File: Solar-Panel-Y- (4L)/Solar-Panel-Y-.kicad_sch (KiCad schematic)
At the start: 77 parts, among them J1 FTS-105-01-L-DV-A, J2 BM02B-SRSS-TB, Q1 BSS138DWQ-7, Q2 MBT2222ADW1T1, Q3 BSS138DWQ-7, Q4 MBT2222ADW1T1, SW1 D2F-L2-A1, SW2 D2F-L2-A, U1 BQ25570RGRR, U2 TSL2561

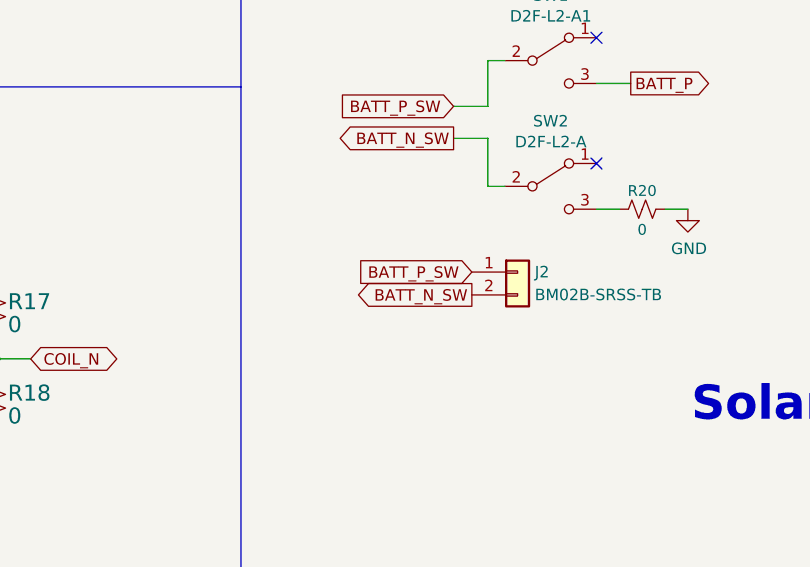
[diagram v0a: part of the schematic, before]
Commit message: Z- board antenna updates
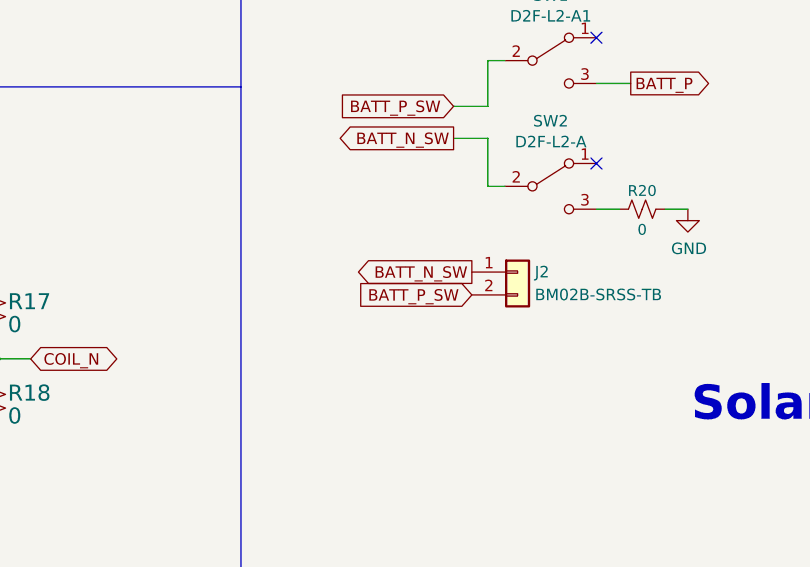
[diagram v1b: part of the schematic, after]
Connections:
- net BATT_N_SW: now also J2.1 (Pin_1); no longer J2.2 (Pin_2)
- net BATT_P_SW: now also J2.2 (Pin_2); no longer J2.1 (Pin_1)
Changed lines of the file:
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@@
     )
   )
-  (global_label "BATT_N_SW" (shape output) (at 234.442 168.148 180) (fields_autoplaced)
+  (global_label "BATT_N_SW" (shape output) (at 234.442 165.608 180) (fields_autoplaced)
     (effects (font (size 1.27 1.27)) (justify right))
-    (property "Intersheet References" "${INTERSHEET_REFS}" (id 0) (at 221.8973 168.2274 0)
+    (property "Intersheet References" "${INTERSHEET_REFS}" (id 0) (at 221.8973 165.6874 0)
       (effects (font (size 1.27 1.27)) (justify right) hide)
     )
@@
     )
   )
-  (global_label "BATT_P_SW" (shape input) (at 234.442 165.608 180) (fields_autoplaced)
+  (global_label "BATT_P_SW" (shape input) (at 234.442 168.148 180) (fields_autoplaced)
     (effects (font (size 1.27 1.27)) (justify right))
-    (property "Intersheet References" "${INTERSHEET_REFS}" (id 0) (at 221.9578 165.5286 0)
+    (property "Intersheet References" "${INTERSHEET_REFS}" (id 0) (at 221.9578 168.0686 0)
       (effects (font (size 1.27 1.27)) (justify right) hide)
     )

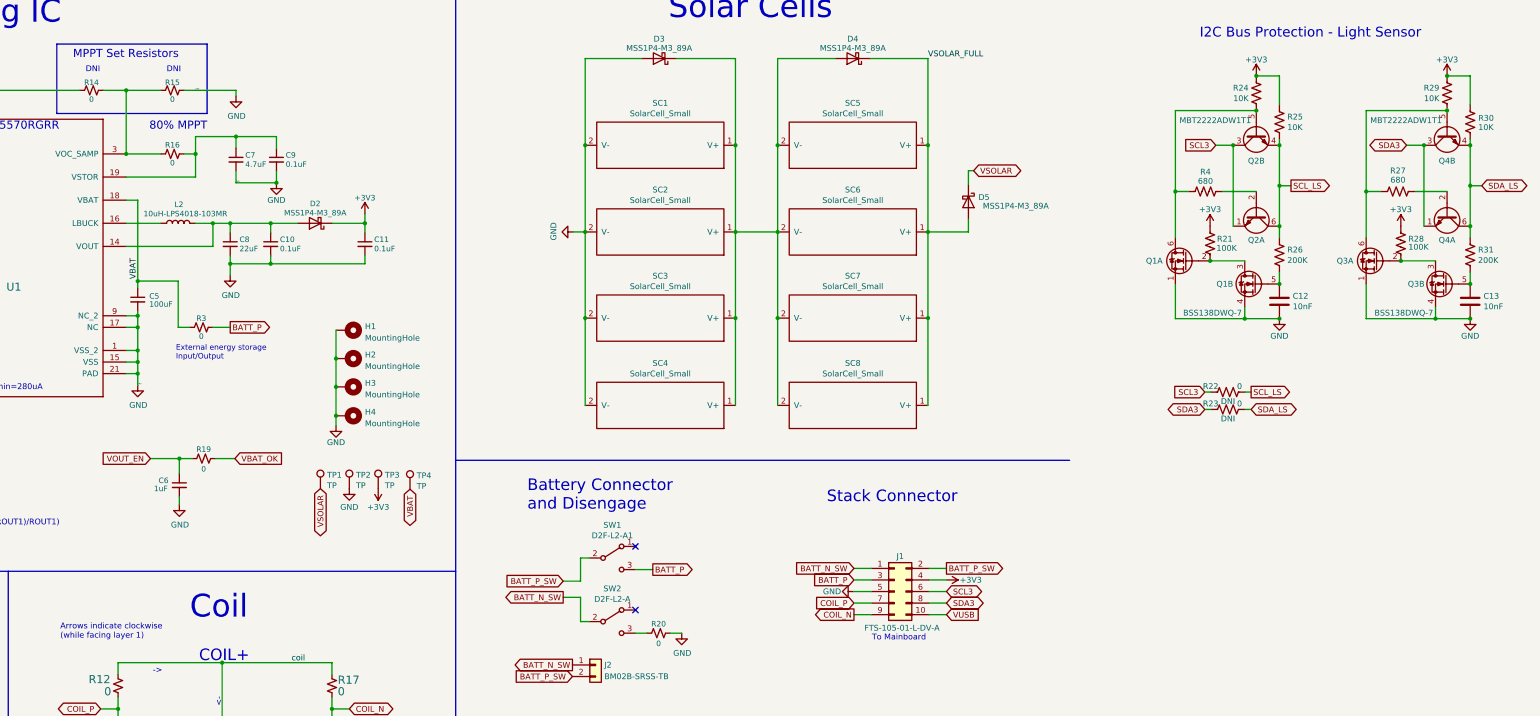
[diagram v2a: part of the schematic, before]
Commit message: Updated all solar panels to Rev B2/01 + Export STEP / BOM
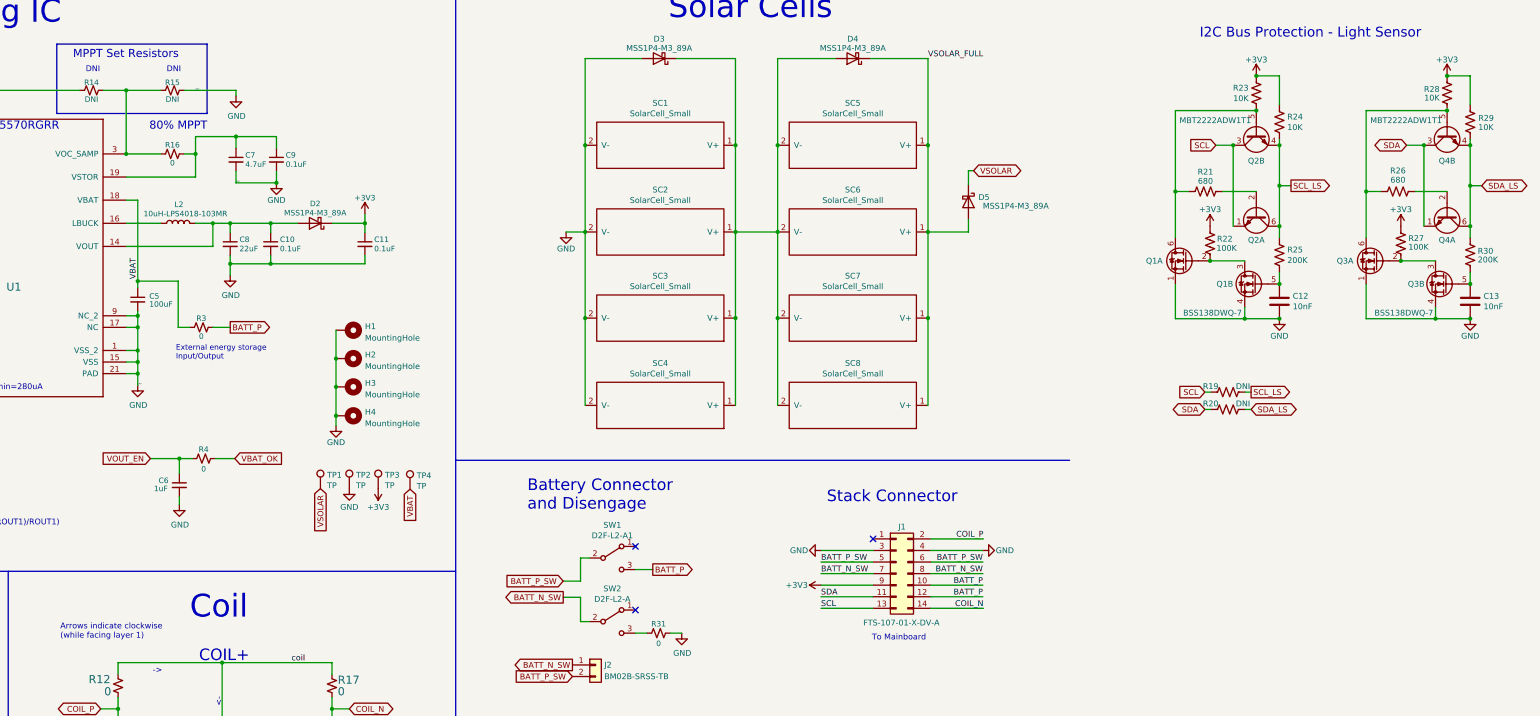
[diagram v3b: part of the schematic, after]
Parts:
- removed J1: FTS-105-01-L-DV-A, batteryboard:FTS-105-XX-YY-DV-A, symbol Connector_Generic:Conn_02x05_Odd_Even
- added J1: FTS-107-01-X-DV-A, batteryboard:SAMTEC-FTS-107-01-X-DV-A, symbol Connector_Generic:Conn_02x07_Odd_Even
- C10, C11, C12, C13, C2, C3, C4, C6, C7, C8, C9: footprint Capacitor_SMD:C_0402_1005Metric -> Capacitor_SMD:C_0603_1608Metric
- R10, R11, R12, R13, R16, R17, R18, R3, R5, R6, R7, R8, R9: footprint Resistor_SMD:R_0402_1005Metric -> Resistor_SMD:R_0603_1608Metric
- R14, R15: value 0 -> DNI; footprint Resistor_SMD:R_0402_1005Metric -> Resistor_SMD:R_0603_1608Metric
- R19: renamed from R22; value 0 -> DNI; footprint Resistor_SMD:R_0402_1005Metric -> Resistor_SMD:R_0603_1608Metric
- R20: renamed from R23; value 0 -> DNI; footprint Resistor_SMD:R_0402_1005Metric -> Resistor_SMD:R_0603_1608Metric
- R21: renamed from R4; footprint Resistor_SMD:R_0402_1005Metric -> Resistor_SMD:R_0603_1608Metric
- R22: renamed from R21; footprint Resistor_SMD:R_0402_1005Metric -> Resistor_SMD:R_0603_1608Metric
- R23: renamed from R24; footprint Resistor_SMD:R_0402_1005Metric -> Resistor_SMD:R_0603_1608Metric
- R24: renamed from R25; footprint Resistor_SMD:R_0402_1005Metric -> Resistor_SMD:R_0603_1608Metric
- R25: renamed from R26; footprint Resistor_SMD:R_0402_1005Metric -> Resistor_SMD:R_0603_1608Metric
- R26: renamed from R27; footprint Resistor_SMD:R_0402_1005Metric -> Resistor_SMD:R_0603_1608Metric
- R27: renamed from R28; footprint Resistor_SMD:R_0402_1005Metric -> Resistor_SMD:R_0603_1608Metric
- R28: renamed from R29; footprint Resistor_SMD:R_0402_1005Metric -> Resistor_SMD:R_0603_1608Metric
- R29: renamed from R30; footprint Resistor_SMD:R_0402_1005Metric -> Resistor_SMD:R_0603_1608Metric
- R30: renamed from R31; footprint Resistor_SMD:R_0402_1005Metric -> Resistor_SMD:R_0603_1608Metric
- R31: renamed from R20; footprint Resistor_SMD:R_0402_1005Metric -> Resistor_SMD:R_0603_1608Metric
- R4: renamed from R19; footprint Resistor_SMD:R_0402_1005Metric -> Resistor_SMD:R_0603_1608Metric
- renumbered SC3 to SC2, SC2 to SC3
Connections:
- net +3V3: now also J1.9 (Pin_9)
- net BATT_N_SW: now also J1.7 (Pin_7), J1.8 (Pin_8)
- net BATT_P: now also J1.10 (Pin_10), J1.12 (Pin_12)
- net BATT_P_SW: now also J1.5 (Pin_5), J1.6 (Pin_6)
- net COIL_N: now also J1.14 (Pin_14)
- net COIL_P: now also J1.2 (Pin_2)
- net GND: now also J1.3 (Pin_3), J1.4 (Pin_4)
- net SCL3 renamed SCL
- net SCL: now also J1.13 (Pin_13)
- net SDA3 renamed SDA
- net SDA: now also J1.11 (Pin_11)
- no-connect marks 3 -> 4
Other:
- moved on the sheet: SC2, SC3

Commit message: Y- board changes for Rev B3/01
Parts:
- removed C12, C13: 10nF, Capacitor_SMD:C_0603_1608Metric, symbol Device:C
- removed Q1, Q3: BSS138DWQ-7, Package_TO_SOT_SMD:SOT-363_SC-70-6, symbol mainboard:BSS138DWQ-7
- removed Q2, Q4: MBT2222ADW1T1, Package_TO_SOT_SMD:SOT-363_SC-70-6, symbol Transistor_BJT:MBT2222ADW1T1
- removed R19, R20: DNI, Resistor_SMD:R_0603_1608Metric, symbol Device:R_US
- removed R21, R26: 680, Resistor_SMD:R_0603_1608Metric, symbol Device:R_US
- removed R22, R27: 100K, Resistor_SMD:R_0603_1608Metric, symbol Device:R_US
- removed R23, R24, R28, R29: 10K, Resistor_SMD:R_0603_1608Metric, symbol Device:R_US
- removed R25, R30: 200K, Resistor_SMD:R_0603_1608Metric, symbol Device:R_US
- added C14: 1uF, Capacitor_SMD:C_0603_1608Metric, symbol Device:C_Small
- added R32: 1K, Resistor_SMD:R_0603_1608Metric, symbol Device:R_Small_US
- J2: symbol Connector_Generic:Conn_01x02 -> solarpanels:BM02B-SRSS-TB
- R1, R12, R13, R16, R17, R18, R2, R3, R31, R4: value 0 -> 0R
- R14, R15: value DNI -> DNI (0R)
- U2: value TSL2561 -> BH1750FVI; footprint solarpanels:TSL2561 -> solarpanels:BH1750FVI; symbol solarpanels:symbols_TSL2561 -> solarpanels:BH1750; Height 1.55 -> (none); Manufacturer_Name ams -> (none); Manufacturer_Part_Number TSL2561 -> (none); Mouser Part Number N/A -> (none); Mouser Price/Stock https://www.mouser.com/Search/Refine.aspx?Keyword=N%2FA -> (none)
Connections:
- net +3V3: now also R32.2
- net BATT_P: now also J1.1 (Pin_1), J1.3 (Pin_3); no longer J1.10 (Pin_10), J1.12 (Pin_12)
- net GND: now also J1.10 (Pin_10), J2.MP, U2.7 (GND), C14.1; no longer J1.3 (Pin_3)
- net SCL_LS: now also U2.6 (SCL); no longer U2.4 (SCL)
- net SDA_LS: now also U2.4 (SDA); no longer U2.6 (SDA)
- net at U2.5 (DVI): now also C14.2, R32.1
- no-connect marks 4 -> 3
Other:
- added sheet Bus Protection (BusProtection.kicad_sch)
- note added: "Populate R1 for I2C addr 0x5C, OR Populate R2 for I2C addr 0x23"
- note removed: "I2C Bus Protection - Light Sensor"
- moved on the sheet: C1, R1, R12, R13, R17, R18, R2

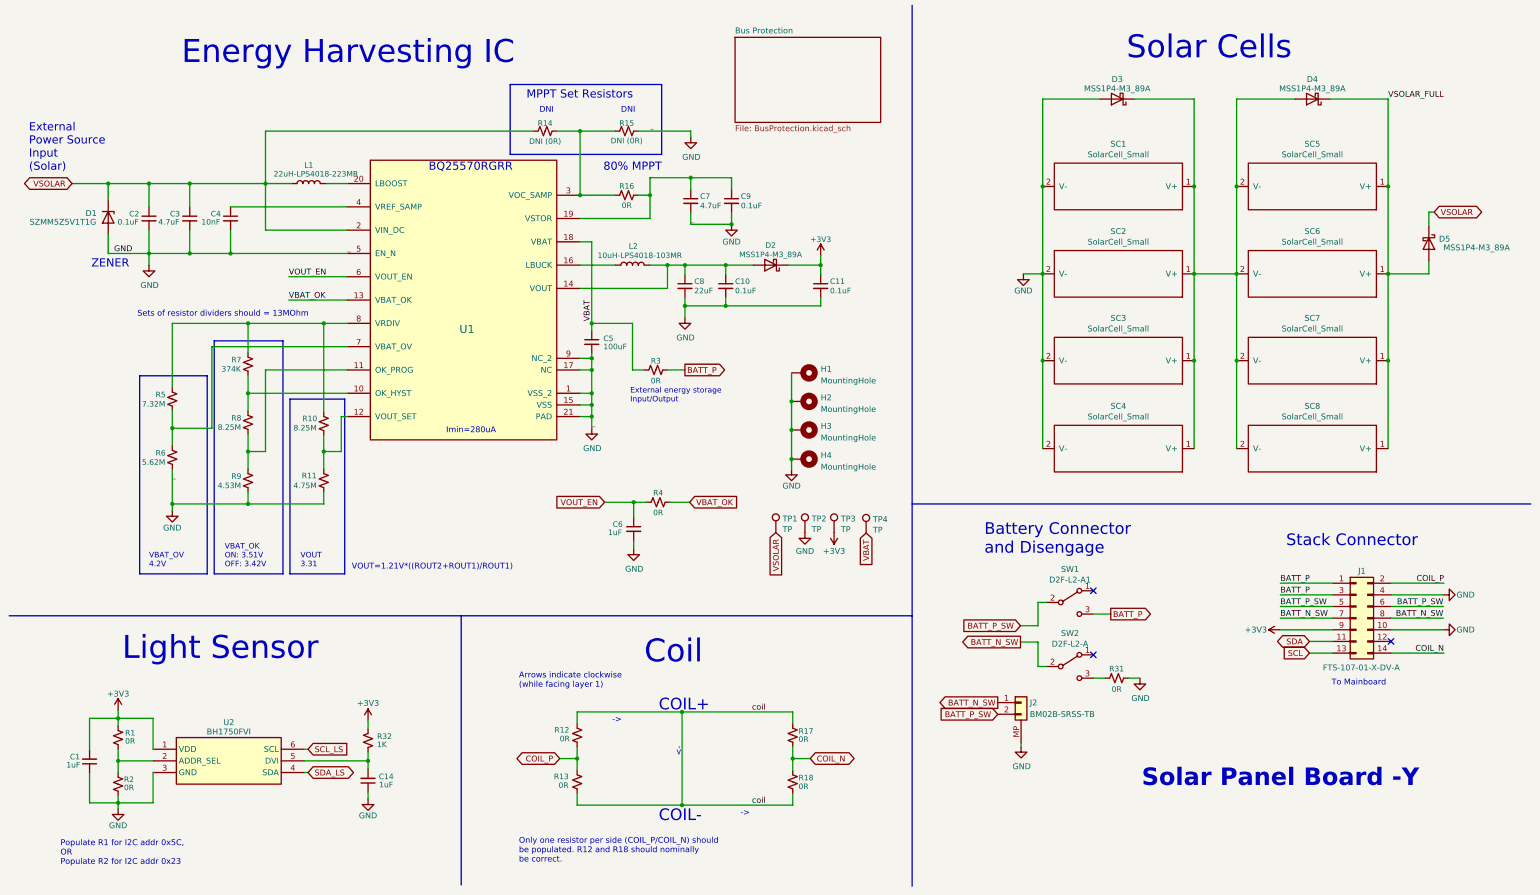
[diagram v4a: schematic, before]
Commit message: Updated light sensor to OPT 3001, Updated solar diodes.
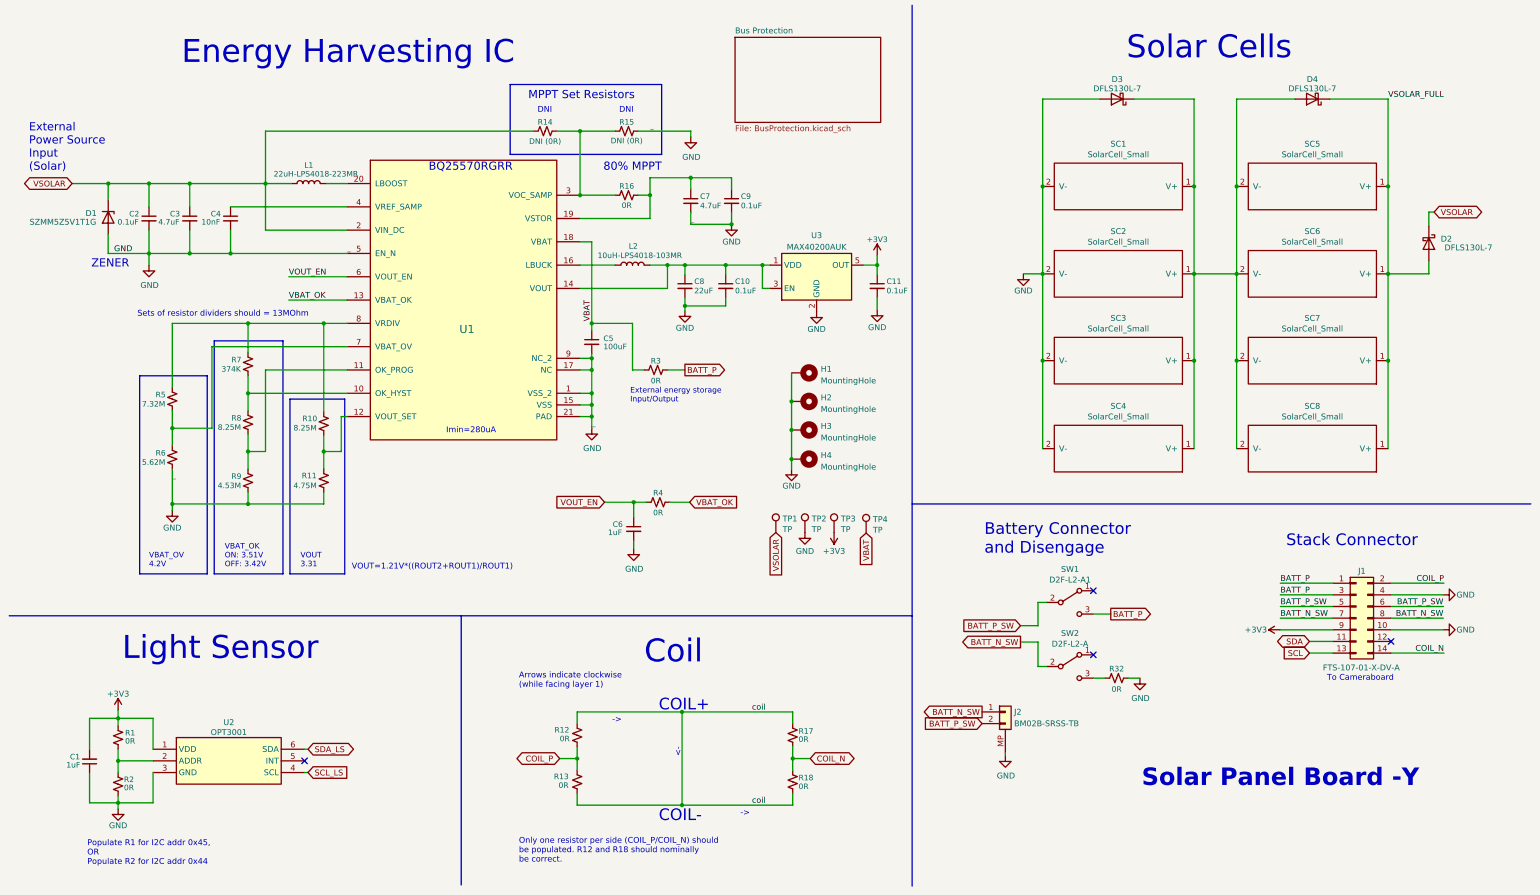
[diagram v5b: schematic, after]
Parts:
- removed C14: 1uF, Capacitor_SMD:C_0603_1608Metric, symbol Device:C_Small
- removed D5: MSS1P4-M3_89A, solarpanels:MICROSMP, symbol Device:D_Schottky
- removed R32: 1K, Resistor_SMD:R_0603_1608Metric, symbol Device:R_Small_US
- removed U2: BH1750FVI, solarpanels:BH1750FVI, symbol solarpanels:BH1750
- added U2: OPT3001, solarpanels:OPT3001, symbol solarpanels:OPT3001
- added U3: MAX40200AUK, Package_TO_SOT_SMD:SOT-23-5, symbol Analog_Switch:MAX40200AUK
- D2, D3, D4: value MSS1P4-M3_89A -> DFLS130L-7; footprint solarpanels:MICROSMP -> Diode_SMD:D_PowerDI-123; Allied Price/Stock https://www.alliedelec.com/general-semiconductor-vishay-mss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 -> (none); Allied_Number 70217632 -> (none); Manufacturer_Name Vishay -> (none); Manufacturer_Part_Number MSS1P4-M3/89A -> (none); Mouser Part Number 625-MSS1P4-M3 -> (none); Mouser Price/Stock https://www.mouser.com/Search/Refine.aspx?Keyword=625-MSS1P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 -> (none); RS Part Number 7103068P -> (none); RS Price/Stock http://uk.rs-online.com/web/p/products/7103068P -> (none)
- renumbered R31 to R32
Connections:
- net +3V3: now also U2.1 (VDD), U3.5 (OUT); no longer D2.1 (K)
- net GND: now also U2.3 (GND), U2.7 (GND), U3.2 (GND)
- net SCL_LS: now also U2.4 (SCL)
- net SDA_LS: now also U2.6 (SDA)
- net VSOLAR: now also D2.1 (K)
- net VSOLAR_FULL: now also D2.2 (A)
- net at R1.1, R2.2: now also U2.2 (ADDR)
- net at C10.1, C8.1, L2.2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: now also U3.1 (VDD), U3.3 (EN); no longer D2.2 (A)
- no-connect marks 3 -> 4
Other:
- note added: "Populate R1 for I2C addr 0x45, OR Populate R2 for I2C addr 0x44"
- note added: "To Cameraboard"
- note removed: "Populate R1 for I2C addr 0x5C, OR Populate R2 for I2C addr 0x23"
- note removed: "To Mainboard"
- moved on the sheet: C11, J2
